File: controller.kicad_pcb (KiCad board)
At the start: 2 copper layers, 60.5 x 122 mm, 150 parts, among them J1 KYCON_KPJX-4S-S, J10 MicroFit_2x04, J11 Phoenix MPT, J12 MicroFit_2x04, J13 JST_B2B-XH, J14 Phoenix MPT, J16 MLX_1x03, J17 MLX_1x03, J2 MicroFit_2x02, J3 24V/5A OUT, J4 DB25 FEMALE, J5 Phoenix MPT, J6 Phoenix MPT, J7 MicroFit_2x04, J8 Phoenix MPT, J9 Phoenix MPT, K1 OJS-SH-124HMF, Q1 BC847, Q2 IRF9540SPBF, Q3 BC857, Q4 BC847, Q5 BC857, U1 MC78M12CDT-TR, U2 MAX5035BUSA, U3 LM358, U4 74HC245, U5 74HC245, U6 ACSL-6310, U7 ACSL-6310

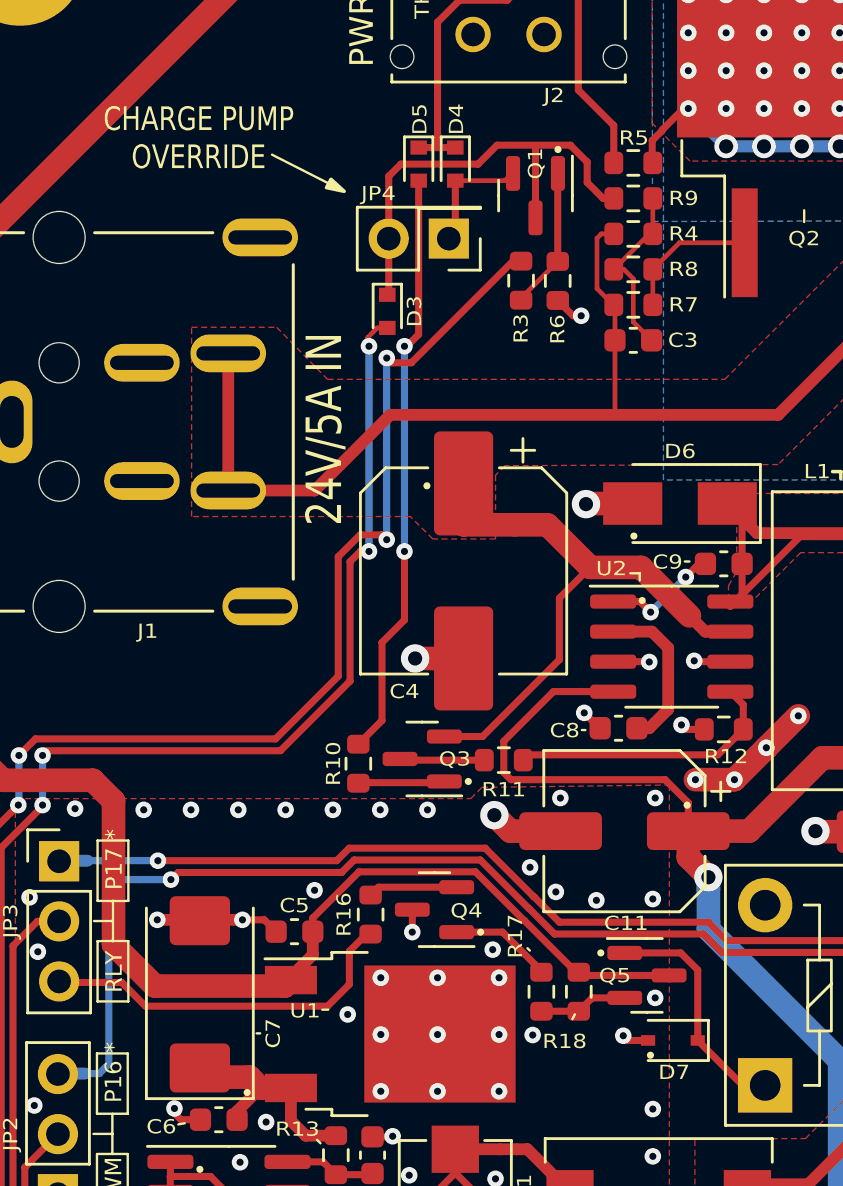
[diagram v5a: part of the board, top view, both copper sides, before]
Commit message: Correct Q5 pin muddle.
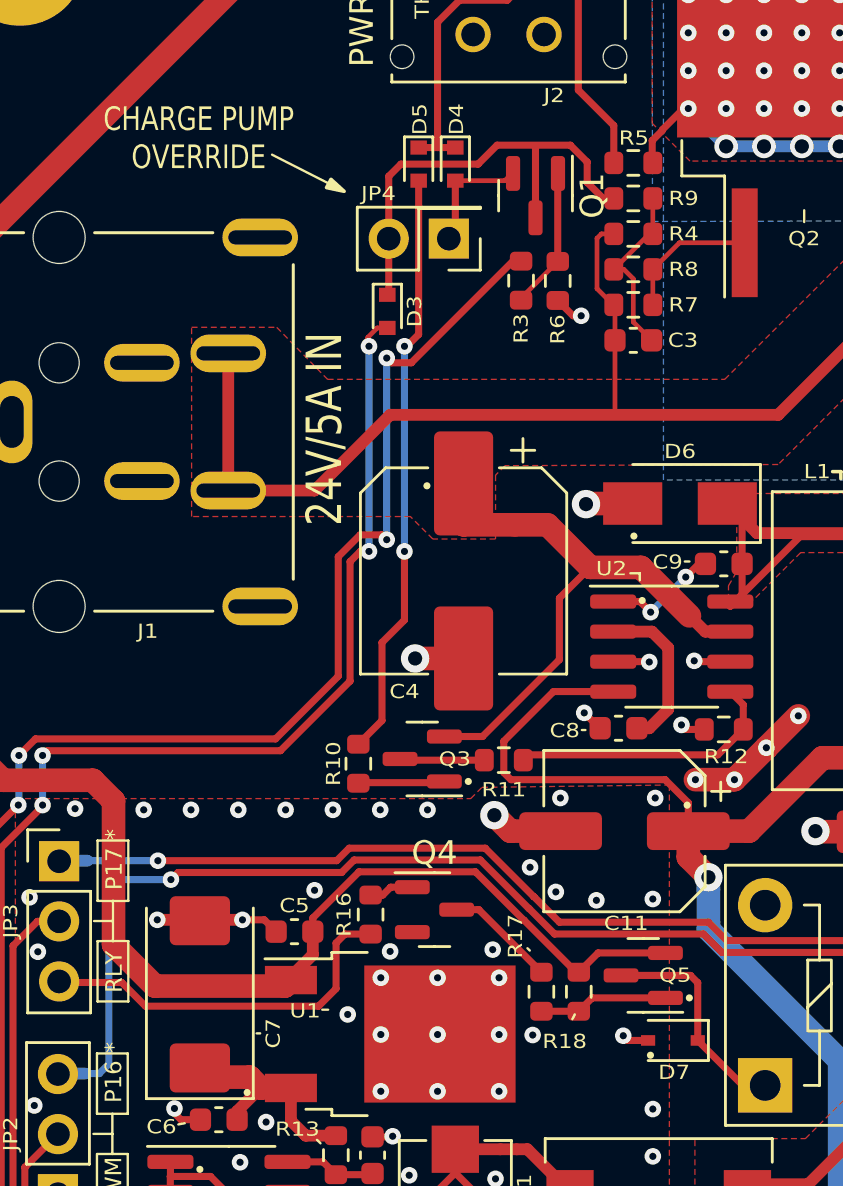
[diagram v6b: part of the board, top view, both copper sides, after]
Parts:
- Q1, Q4: footprint -Project:SOT-23_DOT -> Package_TO_SOT_SMD:SOT-23
- moved Q5 0.16 mm to (87.1, 91.3), turned to 180 degrees
- turned Q4 to 0 degrees
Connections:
- Q4 pad 2: Net-(Q4-Pad2) -> GND
- Q4 pad 3: GND -> Net-(Q4-Pad3)
- Q5 pad 1: Net-(D7-Pad1) -> Net-(Q5-Pad1)
- Q5 pad 2: Net-(Q5-Pad2) -> 24V_SAFE
- Q5 pad 3: 24V_SAFE -> Net-(D7-Pad1)
- R16 pad 1: Net-(Q4-Pad2) -> Net-(Q4-Pad1)
- R17 pad 1: Net-(Q5-Pad2) -> Net-(Q5-Pad1)
- R17 pad 2: Net-(Q4-Pad1) -> Net-(Q4-Pad3)
- R18 pad 2: Net-(Q5-Pad2) -> Net-(Q5-Pad1)
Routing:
- net Net-(Q5-Pad1): track 0.00 -> 5.48 mm
- net Net-(Q4-Pad3): track 0.00 -> 4.68 mm
- net Net-(Q4-Pad2): track 3.78 -> 0.00 mm
- net Net-(Q5-Pad2): track 3.76 -> 0.00 mm
- net Net-(Q4-Pad1): track 4.32 -> 1.90 mm
- net GND: track 85.2 -> 84.2 mm, vias 105 -> 104
- net Net-(D7-Pad1): track 10.0 -> 9.45 mm

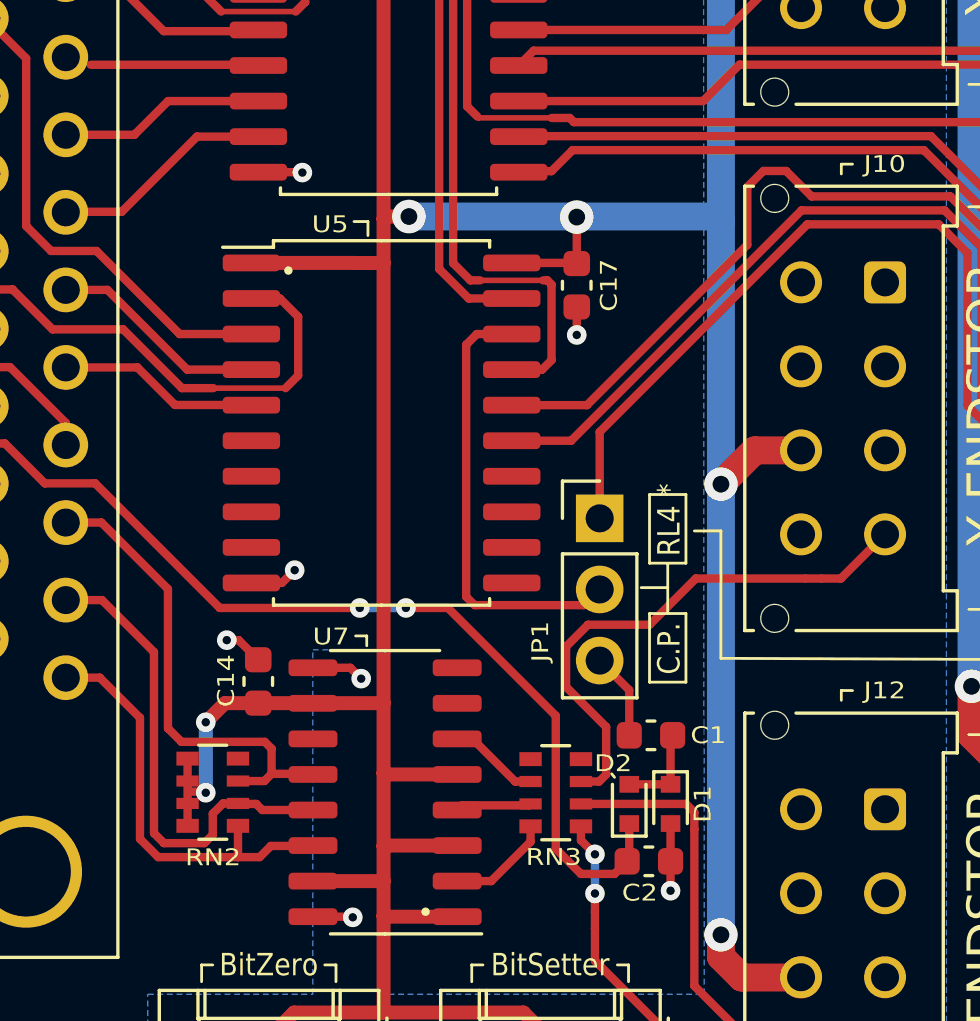
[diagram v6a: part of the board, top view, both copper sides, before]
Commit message: Charge pump signal re-routed.
Funny how the CP signal can't get through if /CE not asserted but /CE can only be asserted if the charge pump signal present. Oops. :/
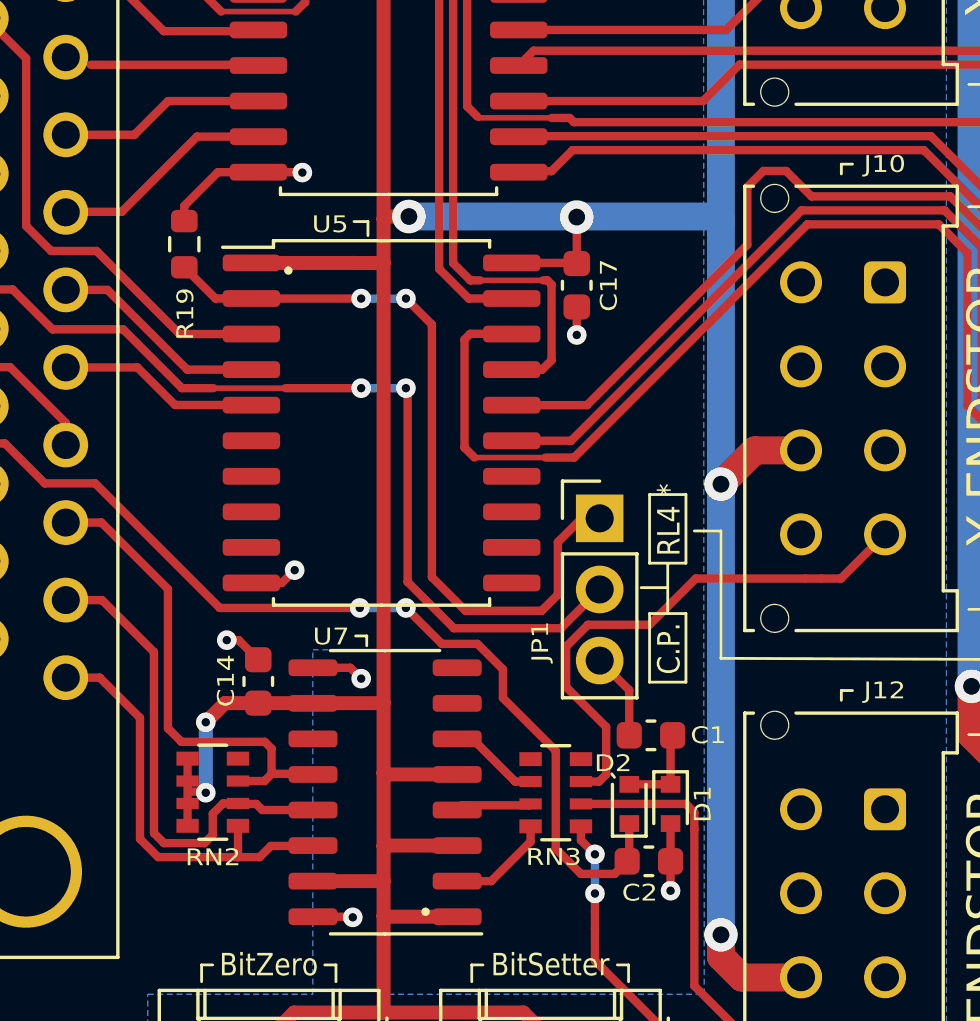
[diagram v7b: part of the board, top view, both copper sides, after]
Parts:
- added R19: 1M, Resistor_SMD:R_0603_1608Metric, F.Cu at (72.5, 133.0)
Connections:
- net /Power/CHARGE_PUMP_IN renamed /LPT Interface/CHARGE_PUMP_OUT
- JP1 pad 1: /Connectors/RELAY4_IN -> Net-(JP1-Pad1)
- JP1 pad 2: /LPT Interface/P1_OUT -> /LPT Interface/P1_IN
- U5 pad 18: /LPT Interface/P1_OUT -> /Connectors/RELAY4_IN
- U5 pad 2: /LPT Interface/P1_IN -> Net-(JP1-Pad1)
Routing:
- net Net-(JP1-Pad1): track 0.00 -> 27.7 mm, vias 0 -> 2
- net /LPT Interface/P1_OUT: track 15.9 -> 0.00 mm
- net /LPT Interface/P1_IN: track 41.0 -> 55.7 mm, vias 0 -> 2
- net /Connectors/RELAY4_IN: track 43.1 -> 51.0 mm
- net GND: track 84.2 -> 87.9 mm

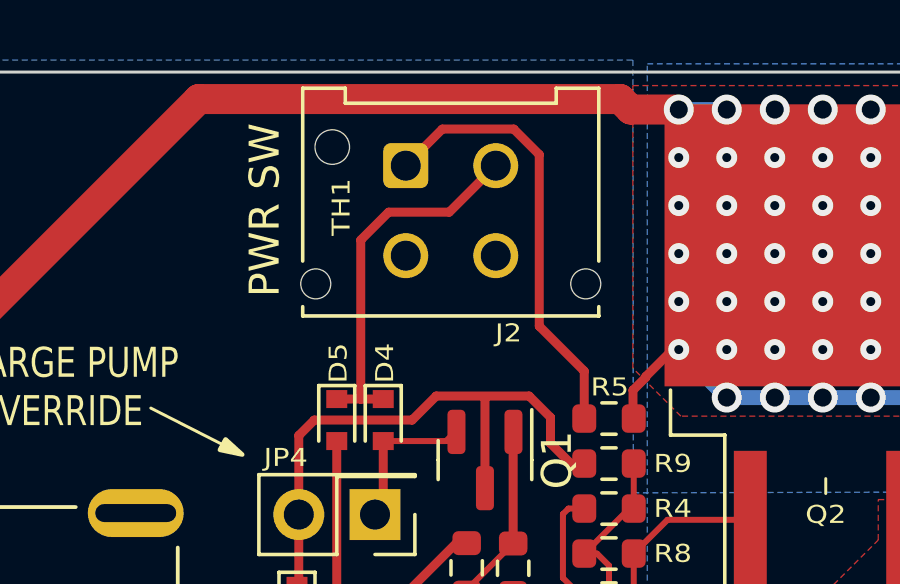
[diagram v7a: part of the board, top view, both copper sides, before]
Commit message: Corrected J2 pinout
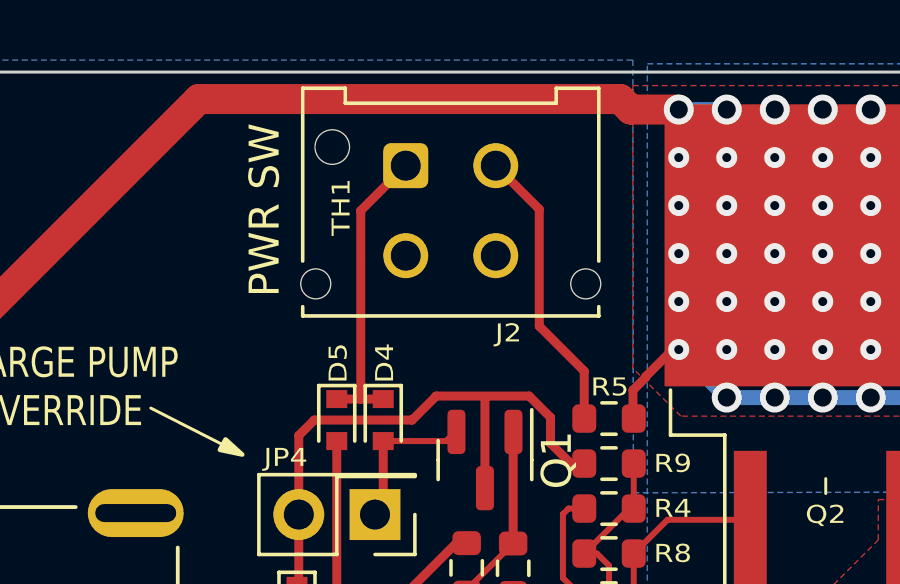
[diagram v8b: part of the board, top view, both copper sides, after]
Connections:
- J2 pad 1: /Power/PLED -> Net-(D4-Pad1)
- J2 pad 2: Net-(D4-Pad1) -> /Power/PLED
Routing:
- net /Power/PLED: track 14.7 -> 9.65 mm
- net Net-(D4-Pad1): track 12.4 -> 9.95 mm
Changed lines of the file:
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@@
     (pad "" np_thru_hole circle (at -3 3.94) (size 1 1) (drill 1) (layers *.Cu *.Mask))
     (pad "1" thru_hole roundrect (at 0 0) (size 1.5 1.5) (drill 1) (layers *.Cu *.Mask) (roundrect_rratio 0.1666673333)
-      (net 118 "/Power/PLED") (pinfunction "Pin_1") (pintype "passive"))
+      (net 144 "Net-(D4-Pad1)") (pinfunction "Pin_1") (pintype "passive"))
     (pad "2" thru_hole circle (at 3 0) (size 1.5 1.5) (drill 1) (layers *.Cu *.Mask)
-      (net 144 "Net-(D4-Pad1)") (pinfunction "Pin_2") (pintype "passive"))
+      (net 118 "/Power/PLED") (pinfunction "Pin_2") (pintype "passive"))
     (pad "3" thru_hole circle (at 0 3) (size 1.5 1.5) (drill 1) (layers *.Cu *.Mask)
       (net 3 "GND") (pinfunction "Pin_3") (pintype "passive"))
@@
   (segment (start 72.98356 129.16644) (end 75.17856 129.16644) (width 0.3) (layer "F.Cu") (net 117))
   (segment (start 69.009331 131.85) (end 70.3 131.85) (width 0.3) (layer "F.Cu") (net 117))
-  (segment (start 85.85 56.95) (end 85.85 55.37) (width 0.3) (layer "F.Cu") (net 118))
-  (segment (start 83.5 47.3) (end 81.12 47.3) (width 0.3) (layer "F.Cu") (net 118))
-  (segment (start 84.35 48.15) (end 83.5 47.3) (width 0.3) (layer "F.Cu") (net 118))
   (segment (start 85.85 55.37) (end 84.35 53.87) (width 0.3) (layer "F.Cu") (net 118))
-  (segment (start 81.12 47.3) (end 79.9 48.52) (width 0.3) (layer "F.Cu") (net 118))
-  (segment (start 84.35 53.87) (end 84.35 48.15) (width 0.3) (layer "F.Cu") (net 118))
+  (segment (start 84.35 49.97) (end 82.9 48.52) (width 0.3) (layer "F.Cu") (net 118))
+  (segment (start 85.85 56.95) (end 85.85 55.37) (width 0.3) (layer "F.Cu") (net 118))
+  (segment (start 84.35 53.87) (end 84.35 49.97) (width 0.3) (layer "F.Cu") (net 118))
   (segment (start 76.05 77.225) (end 76.05 80.525) (width 0.3) (layer "F.Cu") (net 119))
   (segment (start 77 73.375) (end 77 76.275) (width 0.3) (layer "F.Cu") (net 119))
@@
   (segment (start 75.569151 87.902415) (end 76.084385 87.902415) (width 0.3) (layer "F.Cu") (net 143))
   (segment (start 76.084385 87.902415) (end 76.4168 87.57) (width 0.3) (layer "F.Cu") (net 143))
-  (segment (start 78.4 51) (end 78.4 56.3) (width 0.3) (layer "F.Cu") (net 144))
   (segment (start 77.6 56.3) (end 78.4 56.3) (width 0.3) (layer "F.Cu") (net 144))
-  (segment (start 79.33 50.07) (end 78.4 51) (width 0.3) (layer "F.Cu") (net 144))
-  (segment (start 81.35 50.07) (end 79.33 50.07) (width 0.3) (layer "F.Cu") (net 144))
+  (segment (start 79.9 48.52) (end 78.4 50.02) (width 0.3) (layer "F.Cu") (net 144))
+  (segment (start 78.4 50.02) (end 78.4 56.3) (width 0.3) (layer "F.Cu") (net 144))
   (segment (start 78.4 56.3) (end 79.15 56.3) (width 0.3) (layer "F.Cu") (net 144))
-  (segment (start 82.9 48.52) (end 81.35 50.07) (width 0.3) (layer "F.Cu") (net 144))
   (segment (start 78.527 157.027) (end 78.55 157.05) (width 0.3) (layer "F.Cu") (net 145))
   (segment (start 77.129 157.027) (end 78.527 157.027) (width 0.3) (layer "F.Cu") (net 145))
